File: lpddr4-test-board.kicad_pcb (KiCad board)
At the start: 8 copper layers, 117 x 86 mm, 261 parts, among them IC1 TPS54561, IC2 NCP380HMUAJAATBG, IC3 TPD8S009DSMR, J1 0878311420, J2 08B0-1X1T-36-F, J3 DC_SOCKET, J4 WE_629105150521, J5 61300611121, J6 685119134923, J7 1140084168, J8 61300411121, J9 ddr3-sodimm-slot-2-2013289-2, Q1 BC817W, Q2 BSS138APW, Q3 BSS138APW, Q4 BSS138APW, Q5 BSS138APW, Q6 BSS138APW, U1 XC7K70T-FBG484, U10 REF3012AIDBZT, U12 FT2232HQ, U2 ASEM1-100.000MHZ-LC-T, U3 S25FL128SAGNFI000, U4 TPS65296, U5 TPS62823DLCT, U6 DP83848JSQ_NOPB, Y1 ABM8G-25.000MHZ-18-D2Y-T

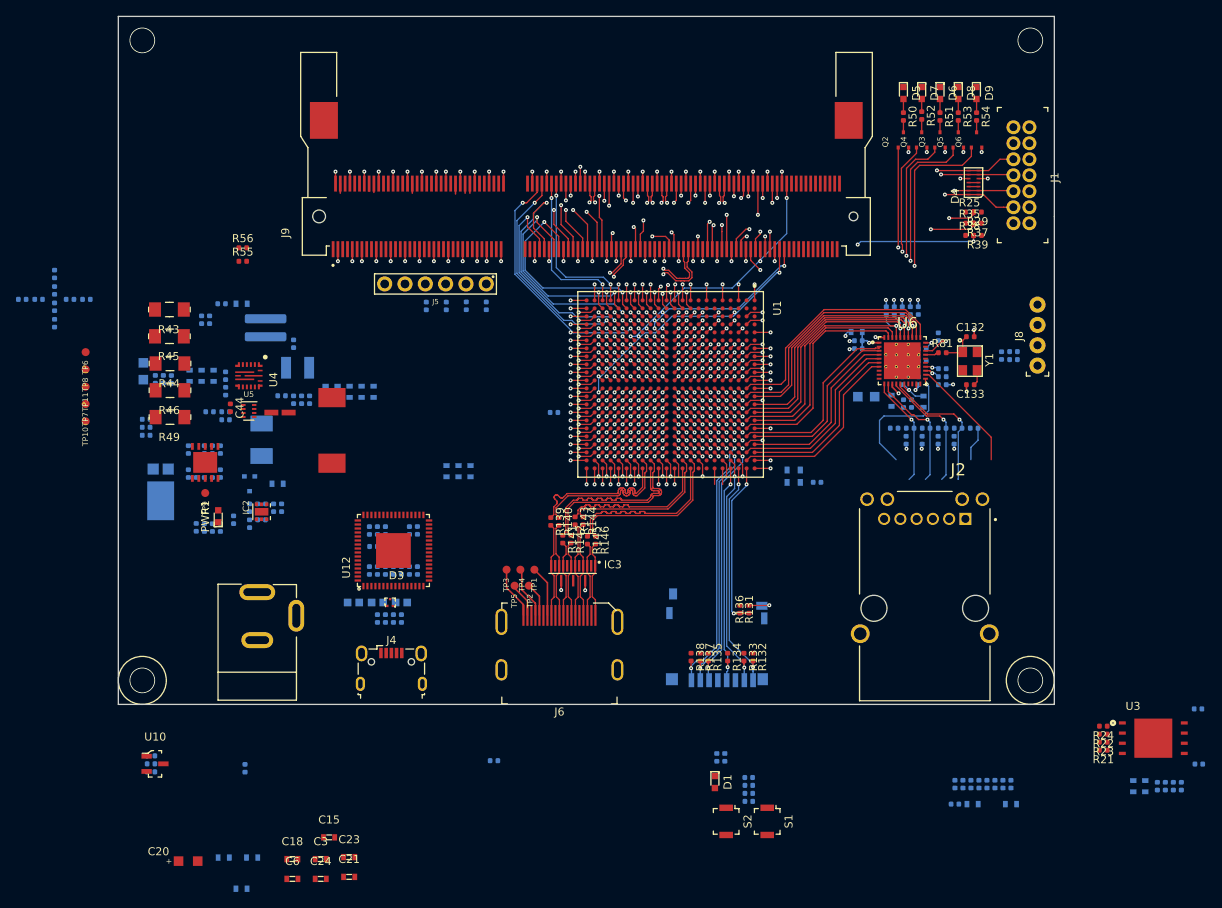
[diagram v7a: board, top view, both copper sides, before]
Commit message: Routed configuration block
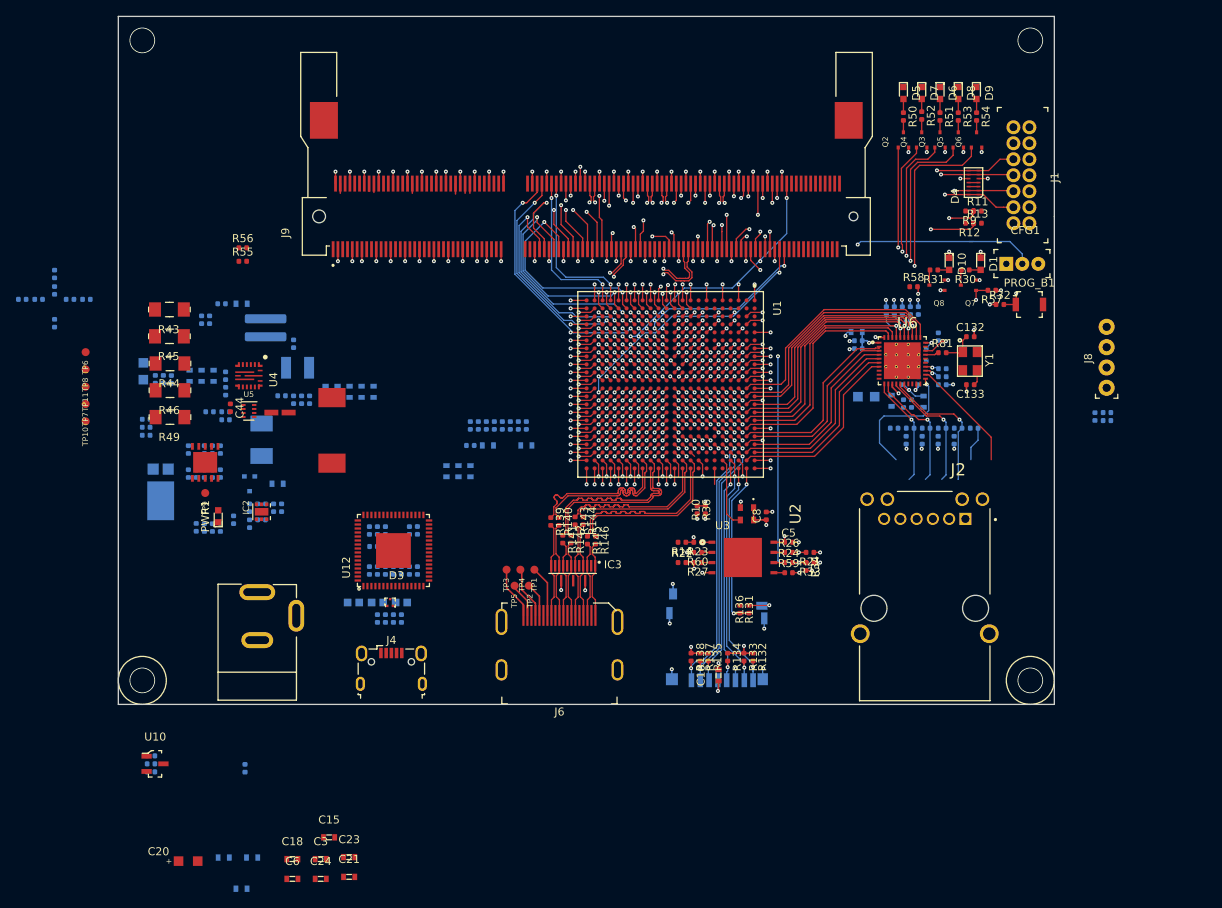
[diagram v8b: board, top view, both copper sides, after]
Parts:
- removed C199: C_100n_0402_6V3, lpddr4-test-board-footprints:0402-cap
- removed J5: 61300611121, lpddr4-test-board-footprints:61300611121
- removed R15, R17: R_200R_0402, lpddr4-test-board-footprints:0402-res
- removed R16: R_10k_0402, lpddr4-test-board-footprints:0402-res
- removed R20: R_4k7_0402, lpddr4-test-board-footprints:0402-res
- removed R25, R29, R35, R37, R38, R39: R_1k_0402, lpddr4-test-board-footprints:0402-res
- removed S1: B3U-1000P, lpddr4-test-board-footprints:Switch_Tactile_SMD_B3U-1000P
- added CFG1: 62000311121, antmicro-footprints:62000311121, F.Cu at (213.0, 80.9)
- added D10: KP-1608CGCK, lpddr4-test-board-footprints:LED_0603, F.Cu at (203.9, 80.9)
- added Q7: BSS138APW, antmicro-footprints:SC70-3, F.Cu at (206.3, 83.6)
- added Q8: BSS138APW, antmicro-footprints:SC70-3, F.Cu at (202.3, 83.6)
- added R57: R_330R_0402, antmicro-footprints:0402-res, F.Cu at (209.2, 84.2)
- added R58: R_0R_0402, antmicro-footprints:0402-res, F.Cu at (199.4, 83.8)
- added R59: R_0R_0402, antmicro-footprints:0402-res, F.Cu at (183.8, 119.5)
- added R60: R_0R_0402, antmicro-footprints:0402-res, F.Cu at (172.4, 117.0)
- C10: value C_100n_0402_6V3 -> C_1u_0603; footprint lpddr4-test-board-footprints:0402-cap -> antmicro-footprints:0603-cap; moved to F.Cu
- C5, C8, R33, R34, U2: moved to F.Cu
- D1: value LG_L29K-G2J1-24-Z -> KP-1608CGCK
- R10: value R_49R9_0402 -> R_100R_0402; moved to F.Cu
- R11, R12, R13, R9: value R_200R_0402 -> R_0R_0402; footprint lpddr4-test-board-footprints:0402-res -> antmicro-footprints:0402-res; moved to F.Cu
- R14: value R_200R_0402 -> R_2k2_0402; footprint lpddr4-test-board-footprints:0402-res -> antmicro-footprints:0402-res; moved to F.Cu
- R21, R22: value R_100R_0402 -> R_4k7_0402
- R23, R24: value R_100R_0402 -> R_0R_0402; footprint lpddr4-test-board-footprints:0402-res -> antmicro-footprints:0402-res
- R26, R27: value R_1k8_0603 -> R_0R_0402; footprint lpddr4-test-board-footprints:0603-res -> antmicro-footprints:0402-res; moved to F.Cu
- R30: value R_200R_0402 -> R_330R_0402; moved to F.Cu
- R31: value R_4k7_0402 -> R_330R_0402; moved to F.Cu
- R32: value R_100R_0402 -> R_4k7_0402; moved to F.Cu
- R36: value R_4k7_0402 -> R_100R_0402; moved to F.Cu
- moved R36 84.2 mm to (172.4, 111.7), turned to 270 degrees
- moved C1 75.4 mm to (144.0, 103.6)
- moved C2 75.4 mm to (146.2, 103.6)
- moved C4 75.4 mm to (151.0, 103.6)
- moved R1 75.4 mm to (144.0, 101.1)
- moved R2 75.4 mm to (145.0, 101.1)
- moved R3 75.4 mm to (146.0, 101.1)
- moved R4 75.4 mm to (147.0, 101.1)
- moved R5 75.4 mm to (148.0, 101.1)
- moved R6 75.4 mm to (149.0, 101.1)
- moved R7 75.4 mm to (150.0, 101.1)
- moved R8 75.4 mm to (151.0, 101.1)
- moved PROG_B1 74.9 mm to (213.9, 86.0), turned to 0 degrees
- moved D1 72.8 mm to (207.8, 80.9)
- moved R30 71.7 mm to (205.9, 81.7)
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- renumbered S2 to PROG_B1
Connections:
- net INIT renamed INIT_B
- D1 pad 1: Net-(D1-Pad1) -> VCC3V3
- D1 pad 2: GND -> Net-(D1-Pad2)
- PROG_B1 pad 1: PROG -> PROGRAM_B
- R10 pad 1: Net-(R10-Pad1) -> VCC3v3
- R10 pad 2: QSPI_SCK -> PUDC_B
- R11 pad 1: Net-(J5-Pad1) -> MODE0
- R11 pad 2: CK_SS -> GND
- R12 pad 1: Net-(J5-Pad2) -> MODE1
- R12 pad 2: CK_MOSI -> VCC3v3
- R13 pad 1: Net-(J5-Pad3) -> MODE1
- R13 pad 2: CK_MISO -> GND
- R14 pad 1: Net-(J5-Pad4) -> FCS_B
- R14 pad 2: CK_SCK -> VCC3v3
- R21 pad 1: Net-(R21-Pad1) -> VCC3v3
- R21 pad 2: QSPI_DQ0 -> QSPI_DQ3
- R22 pad 1: Net-(R22-Pad1) -> VCC3v3
- R22 pad 2: QSPI_DQ1 -> QSPI_DQ2
- R23 pad 2: QSPI_DQ2 -> FCS_B
- R24 pad 2: QSPI_DQ3 -> CCLK
- R26 pad 1: VCC3v3 -> Net-(R26-Pad1)
- R26 pad 2: Net-(R24-Pad1) -> QSPI_DQ3
- R27 pad 1: VCC3v3 -> Net-(R27-Pad1)
- R27 pad 2: Net-(R23-Pad1) -> QSPI_DQ2
- R30 pad 1: VCC3v3 -> Net-(D1-Pad2)
- R30 pad 2: PROG -> Net-(Q7-Pad3)
- R31 pad 1: VCC3v3 -> Net-(D10-Pad2)
- R31 pad 2: DONE -> Net-(Q8-Pad3)
- R32 pad 1: DONE -> VCC3v3
- R32 pad 2: Net-(D1-Pad1) -> PROGRAM_B
- R33 pad 2: QSPI_SCK -> CCLK
- R34 pad 1: QSPI_SCK -> CCLK
- R36 pad 1: VCC3V3 -> PUDC_B
- R36 pad 2: Net-(R36-Pad2) -> GND
- R9 pad 1: Net-(R9-Pad1) -> MODE0
- R9 pad 2: CK_RST -> VCC3v3
- U1 pad AA14: CK_SCK -> Net-(U1-PadAA14)
- U1 pad AA16: CK_MOSI -> Net-(U1-PadAA16)
- U1 pad AB15: Net-(R9-Pad1) -> Net-(U1-PadAB15)
- U1 pad AB16: CK_SS -> Net-(U1-PadAB16)
- U1 pad AB17: CK_MISO -> Net-(U1-PadAB17)
- U1 pad E21: Net-(U1-PadE21) -> GCLK100
- U1 pad F20: UART_TXD_IN -> Net-(U1-PadF20)
- U1 pad G7: QSPI_SCK -> CCLK
- U1 pad J19: Net-(R10-Pad1) -> EMCCLK
- U1 pad K16: GCLK100 -> Net-(U1-PadK16)
- U1 pad L16: QSPI_CS -> FCS_B
- U1 pad L18: UART_RXD_OUT -> Net-(U1-PadL18)
- U1 pad M6: PROG -> PROGRAM_B
- U1 pad M7: Net-(R36-Pad2) -> CFGBVS
- U3 pad 1: QSPI_CS -> Net-(R23-Pad1)
- U3 pad 2: Net-(R22-Pad1) -> Net-(R60-Pad1)
- U3 pad 3: Net-(R23-Pad1) -> Net-(R27-Pad1)
- U3 pad 5: Net-(R21-Pad1) -> Net-(R59-Pad1)
- U3 pad 6: QSPI_SCK -> Net-(R24-Pad1)
- U3 pad 7: Net-(R24-Pad1) -> Net-(R26-Pad1)
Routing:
- net PROGRAM_B: track 0.00 -> 53.8 mm, vias 0 -> 2
- net DONE: track 0.71 -> 50.7 mm, vias 1 -> 2
- net CCLK: track 0.00 -> 39.9 mm, vias 0 -> 3
- net CFGBVS: track 0.00 -> 39.0 mm, vias 0 -> 2
- net INIT_B: track 0.71 -> 39.2 mm, vias 1 -> 2
- net QSPI_DQ0: track 6.00 -> 28.4 mm, vias 1 -> 2
- net QSPI_DQ3: track 7.38 -> 25.6 mm, vias 1 -> 2
- net FCS_B: track 0.00 -> 17.7 mm, vias 0 -> 2
- net VCC3V3: track 36.1 -> 53.2 mm, vias 27 -> 34
- net GND: track 220.7 -> 235.4 mm, vias 187 -> 202
- net QSPI_DQ2: track 7.88 -> 21.2 mm, vias 1 -> 2
- net QSPI_DQ1: track 4.51 -> 17.6 mm, vias 1 -> 2
- net PUDC_B: track 0.71 -> 11.7 mm, vias 1 -> 2
- net GCLK100: track 0.71 -> 8.92 mm, vias 1 -> 0
- net MODE2: track 41.6 -> 49.0 mm, vias 3 -> 2
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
